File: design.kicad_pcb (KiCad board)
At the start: 2 copper layers, 136.2 x 88.1 mm, 170 parts, among them J1 TYPE-C-31-M-12, U1 TTP223, U10 ATtiny1616-S, U2 TTP223, U3 TTP223, U4 TTP223, U5 TTP223, U6 TTP223, U7 TTP223, U8 TTP223, U9 MAX77751CEFG_T

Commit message: Update design.kicad_pcb
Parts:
- C17, C18, C19, C20, C21, C22, C23, C24, C25, D100, D99, J1, JP17, L1, R3, R4, R5, R6, R7, R8, TP10, TP9, U9: moved to F.Cu
- moved JP17 71.1 mm to (61.1, 70.7)
- moved R8 69.2 mm to (62.0, 81.0)
- moved R6 66.5 mm to (63.3, 56.2)
- moved R7 64.9 mm to (64.1, 80.9)
- moved C24 60.9 mm to (66.2, 77.0)
- moved TP10 60.3 mm to (66.5, 104.4)
- moved TP9 60.3 mm to (66.5, 98.3)
- moved C17 58.3 mm to (67.5, 81.5), turned to 0 degrees
- moved J1 54.0 mm to (69.6, 53.0), turned to 180 degrees
- moved U9 53.2 mm to (70.0, 78.1)
- moved C18 51.2 mm to (71.0, 81.5), turned to 180 degrees
- moved C19 51.2 mm to (71.0, 83.7), turned to 180 degrees
- moved C25 49.6 mm to (71.8, 85.9), turned to 0 degrees
- moved C20 46.4 mm to (73.4, 75.1)
- moved C22 46.4 mm to (73.4, 78.7)
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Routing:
- added copper zone on F.Cu, net +5V
- added copper zone on F.Cu, net GND
- removed copper zone on B.Cu, net +5V
- removed copper zone on B.Cu, net GND

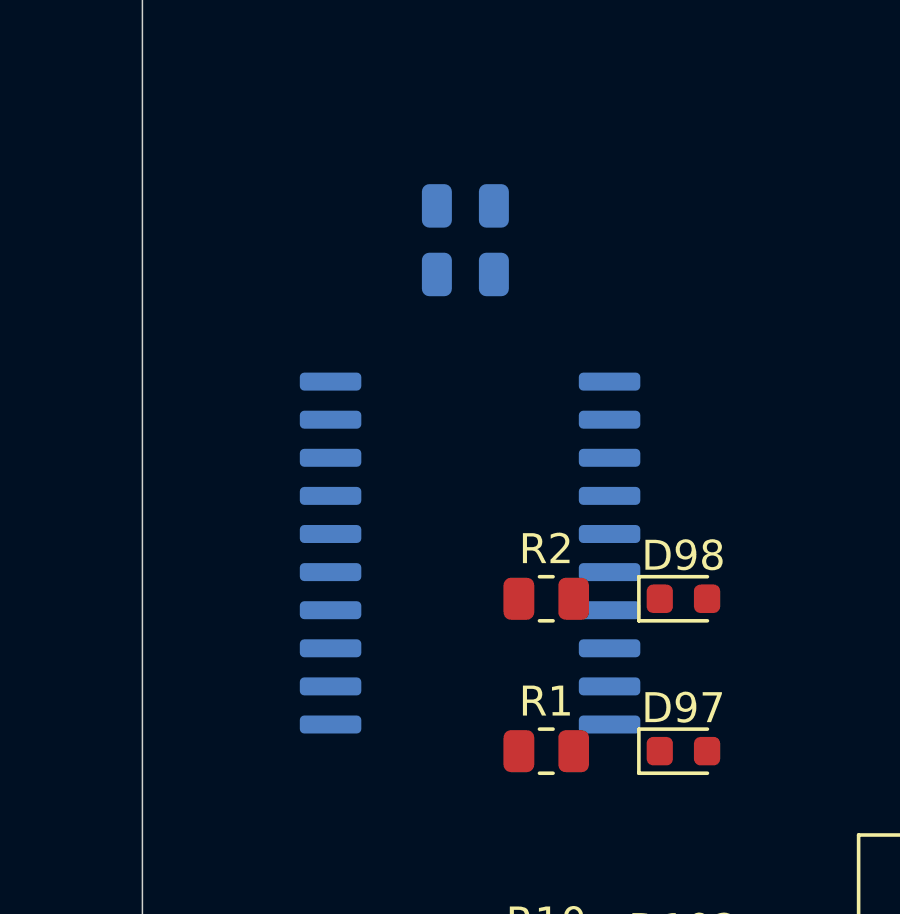
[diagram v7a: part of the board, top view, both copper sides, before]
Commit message: change to QFN 1616
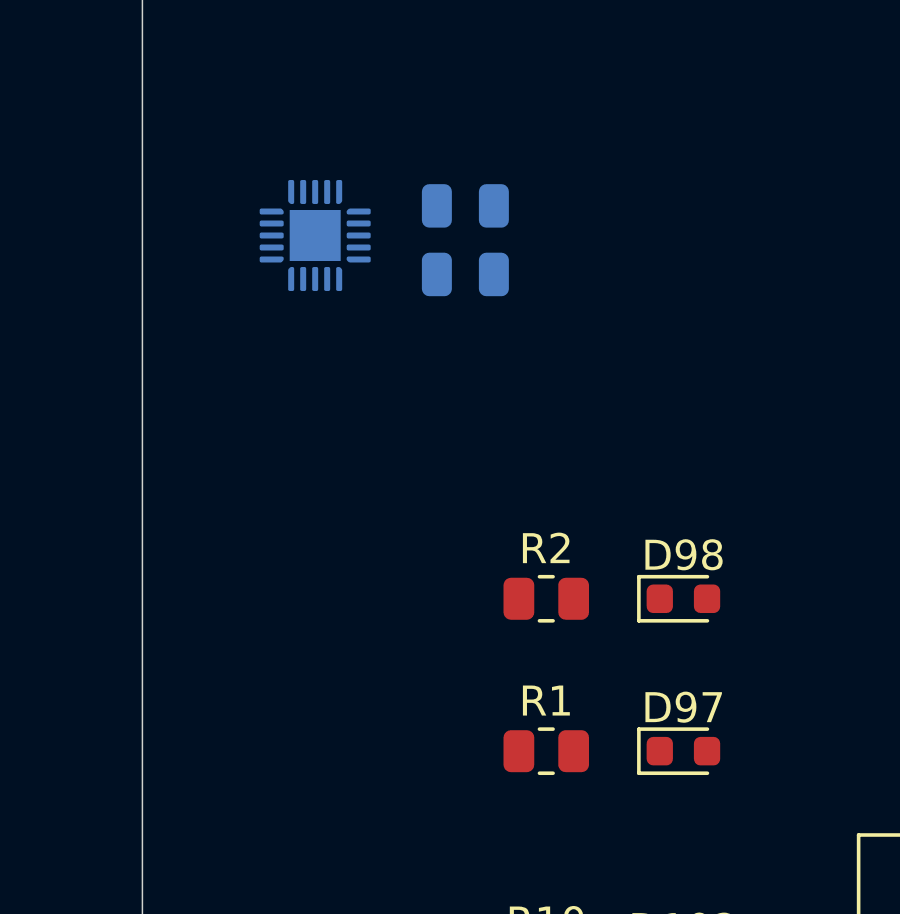
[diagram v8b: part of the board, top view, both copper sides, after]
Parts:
- U10: value ATtiny1616-S -> ATtiny1616-M; footprint Package_SO:SOIC-20W_7.5x12.8mm_P1.27mm -> Package_DFN_QFN:VQFN-20-1EP_3x3mm_P0.4mm_EP1.7x1.7mm
- moved U10 11.8 mm to (115.2, 107.0)
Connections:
- U10 pad 1: +5V -> in
- U10 pad 10: touch_point_4 -> touch_point_7
- U10 pad 11: touch_point_3 -> touch_point_6
- U10 pad 12: Net-(R9-Pad1) -> touch_point_5
- U10 pad 13: Net-(R10-Pad1) -> touch_point_4
- U10 pad 14: unconnected-(U10-Pad14) -> touch_point_3
- U10 pad 15: unconnected-(U10-Pad15) -> Net-(R9-Pad1)
- U10 pad 16: UPDI -> Net-(R10-Pad1)
- U10 pad 18: in -> unconnected-(U10-Pad18)
- U10 pad 19: unconnected-(U10-Pad19) -> UPDI
- U10 pad 20: GND -> unconnected-(U10-Pad20)
- U10 pad 3: unconnected-(U10-Pad3) -> GND
- U10 pad 4: touch_point_1 -> +5V
- U10 pad 5: touch_point_2 -> unconnected-(U10-Pad5)
- U10 pad 6: touch_point_8 -> unconnected-(U10-Pad6)
- U10 pad 7: touch_point_7 -> touch_point_1
- U10 pad 8: touch_point_6 -> touch_point_2
- U10 pad 9: touch_point_5 -> touch_point_8
